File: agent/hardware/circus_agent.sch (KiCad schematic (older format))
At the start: 66 parts, among them J1001 M20-9990345, J1002 M20-9990345, J61 PowerClip, J62 PowerClip, J63 PowerClip, J64 PowerClip, M71 Motor, M81 Motor, Q11 PMV65XPEA, Q12 MMBT2222LT1G, Q21 PMV65XPEA, Q41 PMV65XPEA, Q71 PMV65XPEA, Q72 PMV65XPEA, Q73 MMBT2222LT1G, Q74 IRLML6244TRPBF, Q75 IRLML6244TRPBF, Q76 MMBT2222LT1G, Q81 PMV65XPEA, Q82 PMV65XPEA, Q83 MMBT2222LT1G, Q84 IRLML6244TRPBF, Q85 IRLML6244TRPBF, Q86 MMBT2222LT1G, U1001 C8051F850-C-GU, U21 TSOP38438, U91 LP3985IM5-2.7/NOPB

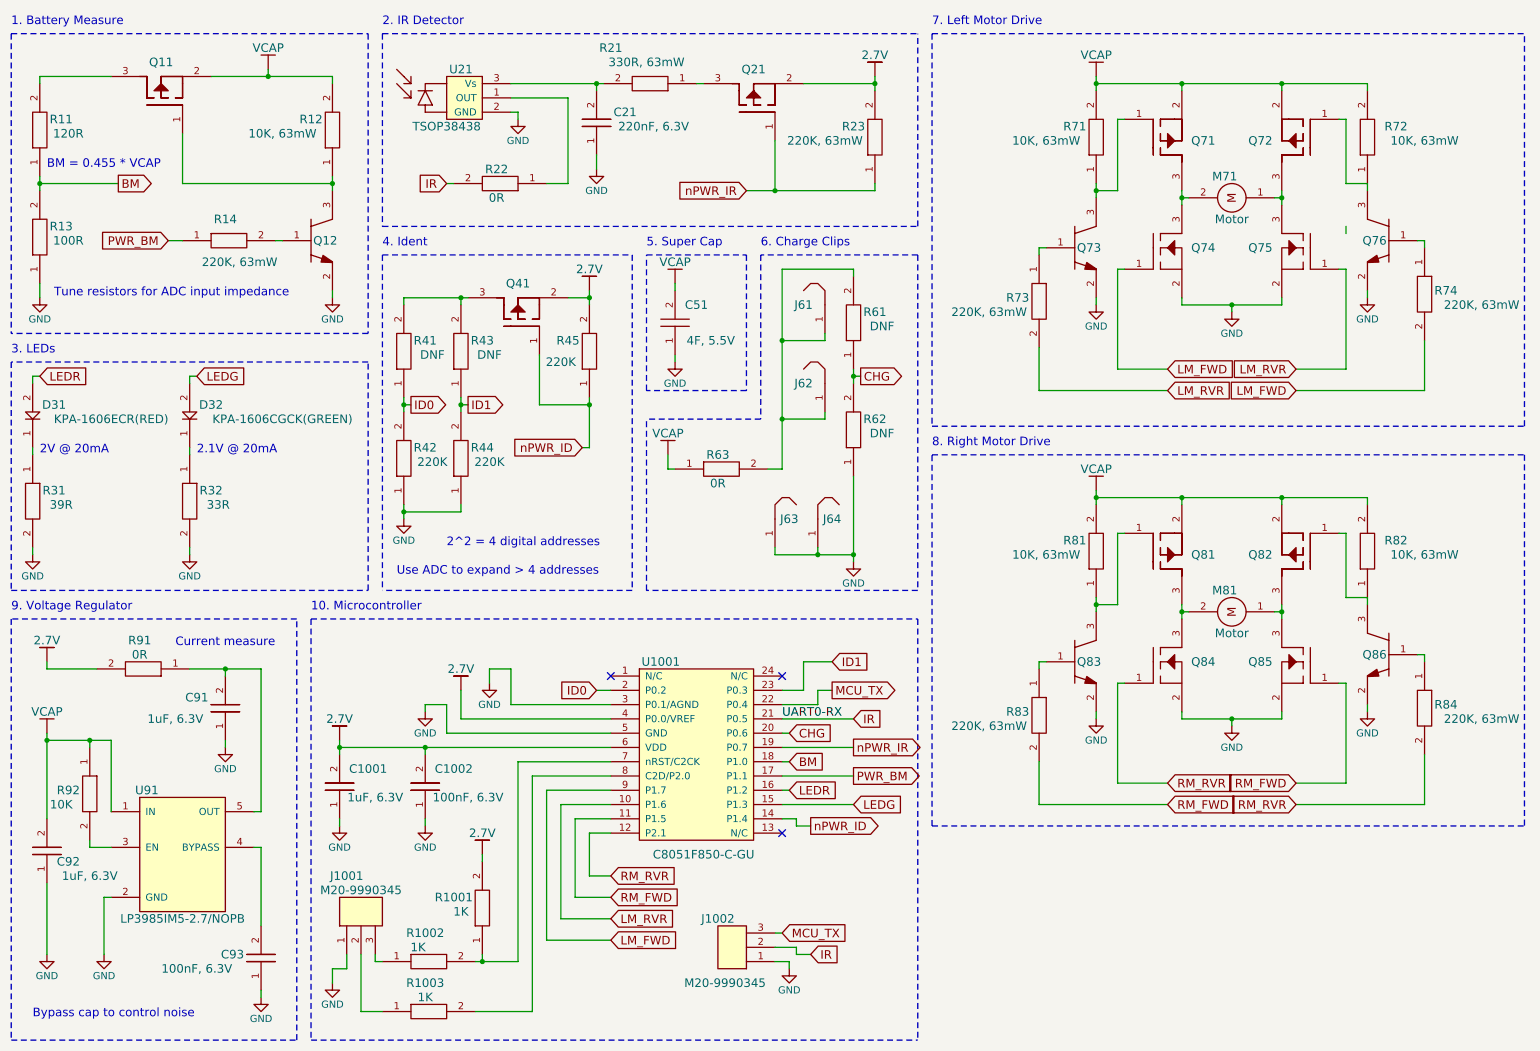
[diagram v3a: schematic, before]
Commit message: updated power rails
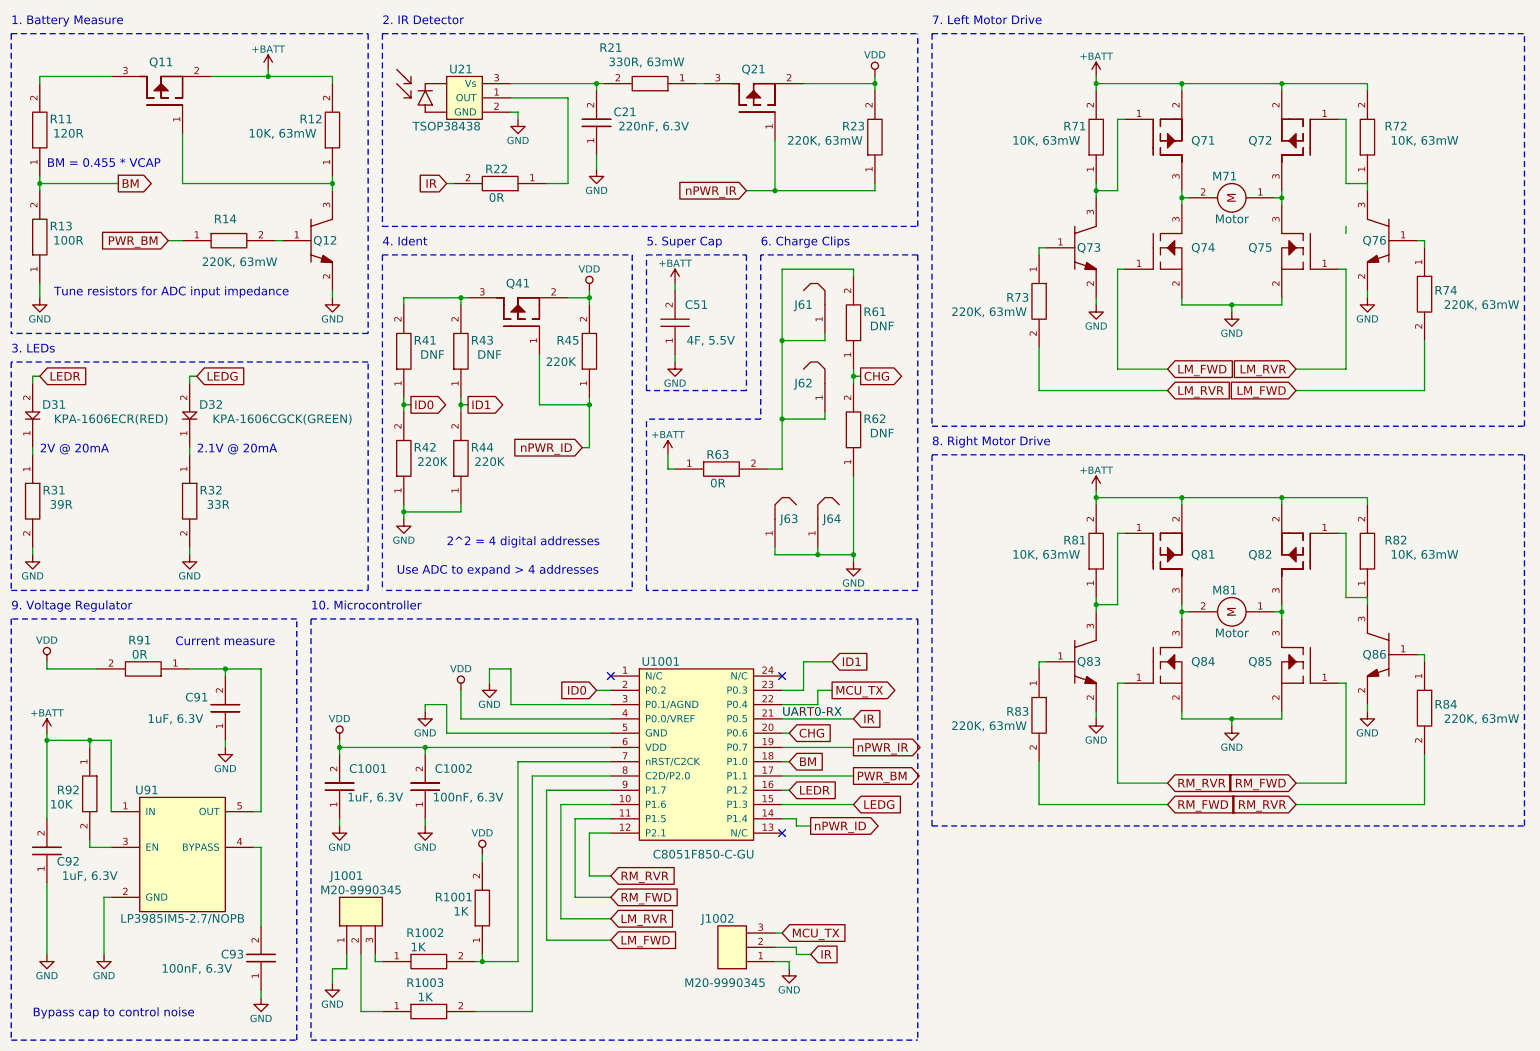
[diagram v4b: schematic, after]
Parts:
- C51: footprint (none) -> circus_agent:SuperCap
- M71, M81: footprint (none) -> circus_agent:Motor
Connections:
- net VDD: now reaches Q21.2, R23.2
- net VDD: now also C1001.2, C1002.2, Q41.2, R1001.2, R45.2, R91.2, U1001.4 (P0.0/VREF), U1001.6 (VDD)
- net +BATT: now reaches Q71.2, Q72.2, R71.2, R72.2
- net +BATT: now also C51.2, C92.2, Q11.2, Q81.2, Q82.2, R12.2, R63.1, R81.2, R82.2, R92.1, U91.1 (IN)
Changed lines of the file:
@@
-$EndComp
-$Comp
-L VCAP #PWR03
-U 1 1 5B333F06
-P 8100 950
-F 0 "#PWR03" H 8400 1100 60  0001 C CNN
-F 1 "VCAP" H 8150 1100 60  0000 C CNN
-F 2 "" H 8100 950 60  0001 C CNN
-F 3 "" H 8100 950 60  0001 C CNN
-	1    8100 950
-	1    0    0    -1
 $EndComp
 $Comp
@@
 F 0 "M71" V 8750 1950 60  0000 C CNN
 F 1 "Motor" V 9050 2000 60  0000 C CNN
-F 2 "" H 8600 1650 60  0001 C CNN
+F 2 "circus_agent:Motor" H 8600 1650 60  0001 C CNN
 F 3 "" H 8600 1650 60  0001 C CNN
 	1    8800 1700
@@
 $EndComp
 $Comp
-L VCAP #PWR07
-U 1 1 5B354D0D
-P 8100 3850
-F 0 "#PWR07" H 8400 4000 60  0001 C CNN
-F 1 "VCAP" H 8150 4000 60  0000 C CNN
-F 2 "" H 8100 3850 60  0001 C CNN
-F 3 "" H 8100 3850 60  0001 C CNN
-	1    8100 3850
-	1    0    0    -1
-$EndComp
-$Comp
 L PMV65XPEA Q82
 U 1 1 5B354D15
@@
 F 0 "M81" V 8750 4850 60  0000 C CNN
 F 1 "Motor" V 9050 4900 60  0000 C CNN
-F 2 "" H 8600 4550 60  0001 C CNN
+F 2 "circus_agent:Motor" H 8600 4550 60  0001 C CNN
 F 3 "" H 8600 4550 60  0001 C CNN
 	1    8800 4600
@@
 $EndComp
 $Comp
-L VCAP #PWR013
-U 1 1 5B35AF65
-P 5150 2400
-F 0 "#PWR013" H 5450 2550 60  0001 C CNN
-F 1 "VCAP" H 5200 2550 60  0000 C CNN
-F 2 "" H 5150 2400 60  0001 C CNN
-F 3 "" H 5150 2400 60  0001 C CNN
-	1    5150 2400
-	1    0    0    -1
-$EndComp
-$Comp
 L PMV65XPEA Q11
 U 1 1 5B35B5AF
@@
 $EndComp
 $Comp
-L VCAP #PWR016
-U 1 1 5B35D64C
-P 2300 900
-F 0 "#PWR016" H 2600 1050 60  0001 C CNN
-F 1 "VCAP" H 2350 1050 60  0000 C CNN
-F 2 "" H 2300 900 60  0001 C CNN
-F 3 "" H 2300 900 60  0001 C CNN
-	1    2300 900
-	1    0    0    -1
-$EndComp
-$Comp
 L CRCW0402330RFKED R14
 U 1 1 5B35E52F
@@
 F 3 "" H 1250 6850 60  0001 C CNN
 	1    1250 6850
-	1    0    0    -1
-$EndComp
-$Comp
-L VCAP #PWR021
-U 1 1 5B3799CB
-P 750 5550
-F 0 "#PWR021" H 1050 5700 60  0001 C CNN
-F 1 "VCAP" H 800 5700 60  0000 C CNN
-F 2 "" H 750 5550 60  0001 C CNN
-F 3 "" H 750 5550 60  0001 C CNN
-	1    750  5550
 	1    0    0    -1
 $EndComp
@@
 Text Notes 1700 4950 0    60   ~ 0
 Current measure
-$Comp
-L 2.7V #PWR026
-U 1 1 5B395992
-P 3650 6400
-F 0 "#PWR026" H 4000 6550 60  0001 C CNN
-F 1 "2.7V" H 3850 6550 60  0000 C CNN
-F 2 "" H 3650 6400 60  0001 C CNN
-F 3 "" H 3650 6400 60  0001 C CNN
-	1    3650 6400
-	1    0    0    -1
-$EndComp
 Text Notes 5800 2150 0    60   ~ 0
 6. Charge Clips
@@
 F 0 "C51" H 5350 3250 60  0000 C CNN
 F 1 "4F, 5.5V" H 5450 3000 60  0000 C CNN
-F 2 "" H 5100 2900 60  0001 C CNN
+F 2 "circus_agent:SuperCap" H 5100 2900 60  0001 C CNN
 F 3 "" H 5100 2900 60  0001 C CNN
 	1    5100 2900
@@
 	0    -1   -1   0
 $EndComp
-$Comp
-L 2.7V #PWR031
-U 1 1 5B3EF4FD
-P 3500 5250
-F 0 "#PWR031" H 3850 5400 60  0001 C CNN
-F 1 "2.7V" H 3700 5400 60  0000 C CNN
-F 2 "" H 3500 5250 60  0001 C CNN
-F 3 "" H 3500 5250 60  0001 C CNN
-	1    3500 5250
-	1    0    0    -1
-$EndComp
-$Comp
-L 2.7V #PWR032
-U 1 1 5B3EF85B
-P 2650 5600
-F 0 "#PWR032" H 3000 5750 60  0001 C CNN
-F 1 "2.7V" H 2850 5750 60  0000 C CNN
-F 2 "" H 2650 5600 60  0001 C CNN
-F 3 "" H 2650 5600 60  0001 C CNN
-	1    2650 5600
-	1    0    0    -1
-$EndComp
-$Comp
-L 2.7V #PWR033
-U 1 1 5B3EFB31
-P 600 5050
-F 0 "#PWR033" H 950 5200 60  0001 C CNN
-F 1 "2.7V" H 800 5200 60  0000 C CNN
-F 2 "" H 600 5050 60  0001 C CNN
-F 3 "" H 600 5050 60  0001 C CNN
-	1    600  5050
-	1    0    0    -1
-$EndComp
-$Comp
-L 2.7V #PWR034
-U 1 1 5B3EFF3C
-P 4400 2450
-F 0 "#PWR034" H 4750 2600 60  0001 C CNN
-F 1 "2.7V" H 4600 2600 60  0000 C CNN
-F 2 "" H 4400 2450 60  0001 C CNN
-F 3 "" H 4400 2450 60  0001 C CNN
-	1    4400 2450
-	1    0    0    -1
-$EndComp
-$Comp
-L 2.7V #PWR035
-U 1 1 5B3F0513
-P 6400 950
-F 0 "#PWR035" H 6750 1100 60  0001 C CNN
-F 1 "2.7V" H 6600 1100 60  0000 C CNN
-F 2 "" H 6400 950 60  0001 C CNN
-F 3 "" H 6400 950 60  0001 C CNN
-	1    6400 950
-	1    0    0    -1
-$EndComp
 Wire Wire Line
 	5900 6950 5950 6950
@@
 F 3 "" H 6450 4350 50  0001 C CNN
 	1    6450 4350
-	-1   0    0    -1
-$EndComp
-$Comp
-L VCAP #PWR037
-U 1 1 5B458338
-P 5200 3600
-F 0 "#PWR037" H 5500 3750 60  0001 C CNN
-F 1 "VCAP" H 5250 3750 60  0000 C CNN
-F 2 "" H 5200 3600 60  0001 C CNN
-F 3 "" H 5200 3600 60  0001 C CNN
-	1    5200 3600
 	-1   0    0    -1
 $EndComp
@@
 $EndComp
 Connection ~ 6450 4300
+$Comp
+L +BATT #PWR?
+U 1 1 5B4AEF05
+P 8150 950
+F 0 "#PWR?" H 8150 800 50  0001 C CNN
+F 1 "+BATT" H 8150 1090 50  0000 C CNN
+F 2 "" H 8150 950 50  0001 C CNN
+F 3 "" H 8150 950 50  0001 C CNN
+	1    8150 950
+	1    0    0    -1
+$EndComp
+$Comp
+L +BATT #PWR?
+U 1 1 5B4AF38E
+P 8150 3850
+F 0 "#PWR?" H 8150 3700 50  0001 C CNN
+F 1 "+BATT" H 8150 3990 50  0000 C CNN
+F 2 "" H 8150 3850 50  0001 C CNN
+F 3 "" H 8150 3850 50  0001 C CNN
+	1    8150 3850
+	1    0    0    -1
+$EndComp
+$Comp
+L +BATT #PWR?
+U 1 1 5B4AFCAA
+P 5150 3600
+F 0 "#PWR?" H 5150 3450 50  0001 C CNN
+F 1 "+BATT" H 5150 3740 50  0000 C CNN
+F 2 "" H 5150 3600 50  0001 C CNN
+F 3 "" H 5150 3600 50  0001 C CNN
+	1    5150 3600
+	1    0    0    -1
+$EndComp
+$Comp
+L +BATT #PWR?
+U 1 1 5B4B02AF
+P 5200 2400
+F 0 "#PWR?" H 5200 2250 50  0001 C CNN
+F 1 "+BATT" H 5200 2540 50  0000 C CNN
+F 2 "" H 5200 2400 50  0001 C CNN
+F 3 "" H 5200 2400 50  0001 C CNN
+	1    5200 2400
+	1    0    0    -1
+$EndComp
+$Comp
+L +BATT #PWR?
+U 1 1 5B4B054E
+P 2350 900
+F 0 "#PWR?" H 2350 750 50  0001 C CNN
+F 1 "+BATT" H 2350 1040 50  0000 C CNN
+F 2 "" H 2350 900 50  0001 C CNN
+F 3 "" H 2350 900 50  0001 C CNN
+	1    2350 900
+	1    0    0    -1
+$EndComp
+$Comp
+L +BATT #PWR?
+U 1 1 5B4B0F89
+P 800 5550
+F 0 "#PWR?" H 800 5400 50  0001 C CNN
+F 1 "+BATT" H 800 5690 50  0000 C CNN
+F 2 "" H 800 5550 50  0001 C CNN
+F 3 "" H 800 5550 50  0001 C CNN
+	1    800  5550
+	1    0    0    -1
+$EndComp
+$Comp
+L VDD #PWR?
+U 1 1 5B4B1823
+P 6600 950
+F 0 "#PWR?" H 6600 800 50  0001 C CNN
+F 1 "VDD" H 6600 1100 50  0000 C CNN
+F 2 "" H 6600 950 50  0001 C CNN
+F 3 "" H 6600 950 50  0001 C CNN
+	1    6600 950
+	1    0    0    -1
+$EndComp
+$Comp
+L VDD #PWR?
+U 1 1 5B4B1C60
+P 4600 2450
+F 0 "#PWR?" H 4600 2300 50  0001 C CNN
+F 1 "VDD" H 4600 2600 50  0000 C CNN
+F 2 "" H 4600 2450 50  0001 C CNN
+F 3 "" H 4600 2450 50  0001 C CNN
+	1    4600 2450
+	1    0    0    -1
+$EndComp
+$Comp
+L VDD #PWR?
+U 1 1 5B4B2474
+P 800 5050
+F 0 "#PWR?" H 800 4900 50  0001 C CNN
+F 1 "VDD" H 800 5200 50  0000 C CNN
+F 2 "" H 800 5050 50  0001 C CNN
+F 3 "" H 800 5050 50  0001 C CNN
+	1    800  5050
+	1    0    0    -1
+$EndComp
+$Comp
+L VDD #PWR?
+U 1 1 5B4B2868
+P 2850 5600
+F 0 "#PWR?" H 2850 5450 50  0001 C CNN
+F 1 "VDD" H 2850 5750 50  0000 C CNN
+F 2 "" H 2850 5600 50  0001 C CNN
+F 3 "" H 2850 5600 50  0001 C CNN
+	1    2850 5600
+	1    0    0    -1
+$EndComp
+$Comp
+L VDD #PWR?
+U 1 1 5B4B2C1B
+P 3700 5250
+F 0 "#PWR?" H 3700 5100 50  0001 C CNN
+F 1 "VDD" H 3700 5400 50  0000 C CNN
+F 2 "" H 3700 5250 50  0001 C CNN
+F 3 "" H 3700 5250 50  0001 C CNN
+	1    3700 5250
+	1    0    0    -1
+$EndComp
+$Comp
+L VDD #PWR?
+U 1 1 5B4B2DB2
+P 3850 6400
+F 0 "#PWR?" H 3850 6250 50  0001 C CNN
+F 1 "VDD" H 3850 6550 50  0000 C CNN
+F 2 "" H 3850 6400 50  0001 C CNN
+F 3 "" H 3850 6400 50  0001 C CNN
+	1    3850 6400
+	1    0    0    -1
+$EndComp
 $EndSCHEMATC

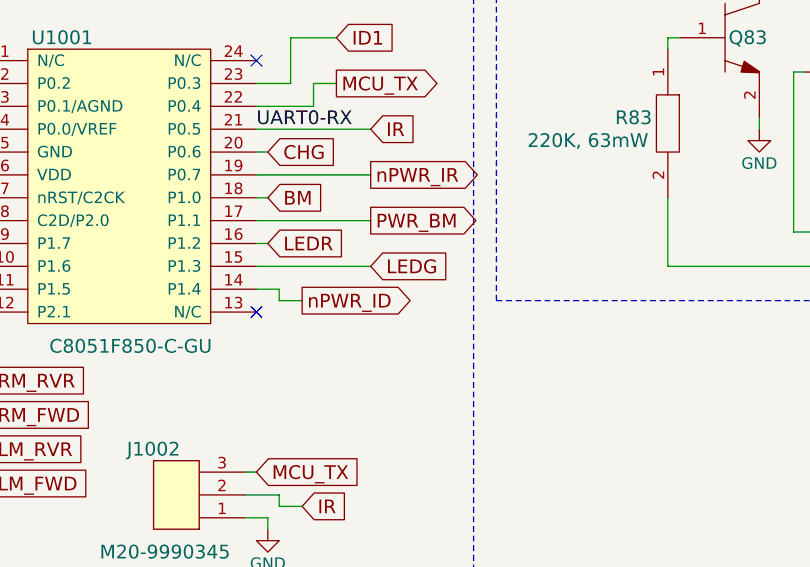
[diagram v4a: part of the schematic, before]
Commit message: First outline for PCB
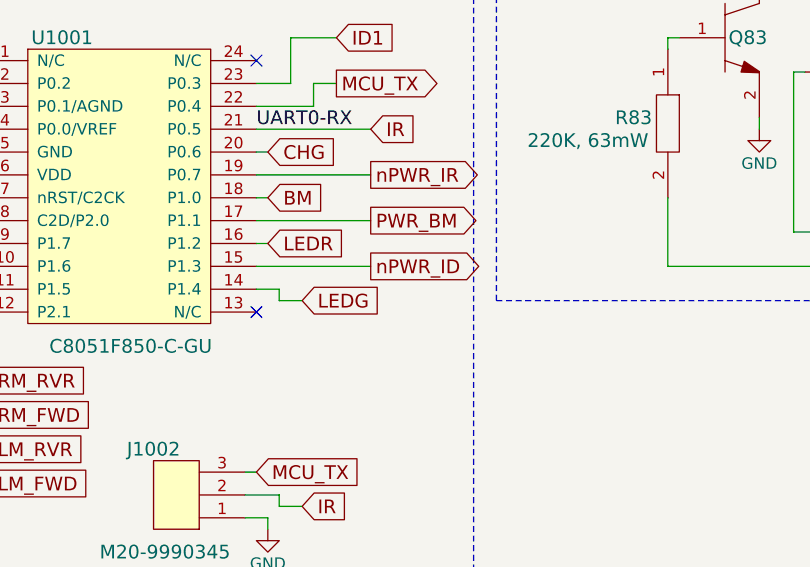
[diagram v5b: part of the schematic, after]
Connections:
- net LEDG: now also U1001.14 (P1.4); no longer U1001.15 (P1.3)
- net nPWR_ID: now also U1001.15 (P1.3); no longer U1001.14 (P1.4)
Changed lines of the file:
@@
 Text GLabel 6450 5650 2    60   Output ~ 0
 nPWR_IR
-Text GLabel 6150 6200 2    60   Output ~ 0
+Text GLabel 6450 6050 2    60   Output ~ 0
 nPWR_ID
 $Comp
@@
 Text GLabel 6000 5950 2    60   Input ~ 0
 LEDR
-Text GLabel 6450 6050 2    60   Input ~ 0
+Text GLabel 6150 6200 2    60   Input ~ 0
 LEDG
 Wire Wire Line
